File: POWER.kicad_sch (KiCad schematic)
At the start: 29 parts, among them J3 BAT_SOCKET, U4 BQ25185, U5 TPS62746, U8 TPS7A0533PDBV

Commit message: Adding outputs, updated some component values.
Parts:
- C11: value C -> 4.7UF
- D3: value D -> BAT54LP
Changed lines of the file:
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@@
 			)
 		)
-		(property "Value" "D"
+		(property "Value" "BAT54LP"
 			(at 181.61 138.43 0)
 			(effects
@@
 			)
 		)
-		(property "Value" "C"
+		(property "Value" "4.7UF"
 			(at 267.97 228.6062 0)
 			(effects

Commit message: removed backup zips. adding updated output files
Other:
- title: nRF Battery Dev Kit -> stm32_bluet_pill
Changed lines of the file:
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@@
 	(paper "A3")
 	(title_block
-		(title "nRF Battery Dev Kit")
-		(date "2024-02-26")
+		(title "stm32_bluet_pill")
+		(date "2024-04-03")
 		(rev "Proto")
 		(company "Clover Designs")

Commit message: updating design files
updating schematics, gerbers, design files, etc.
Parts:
- R16: value 1K -> 2.2K; Tol (none) -> 1%
- R17: Tol (none) -> 1%
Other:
- moved on the sheet: C25, L4, R17, R19

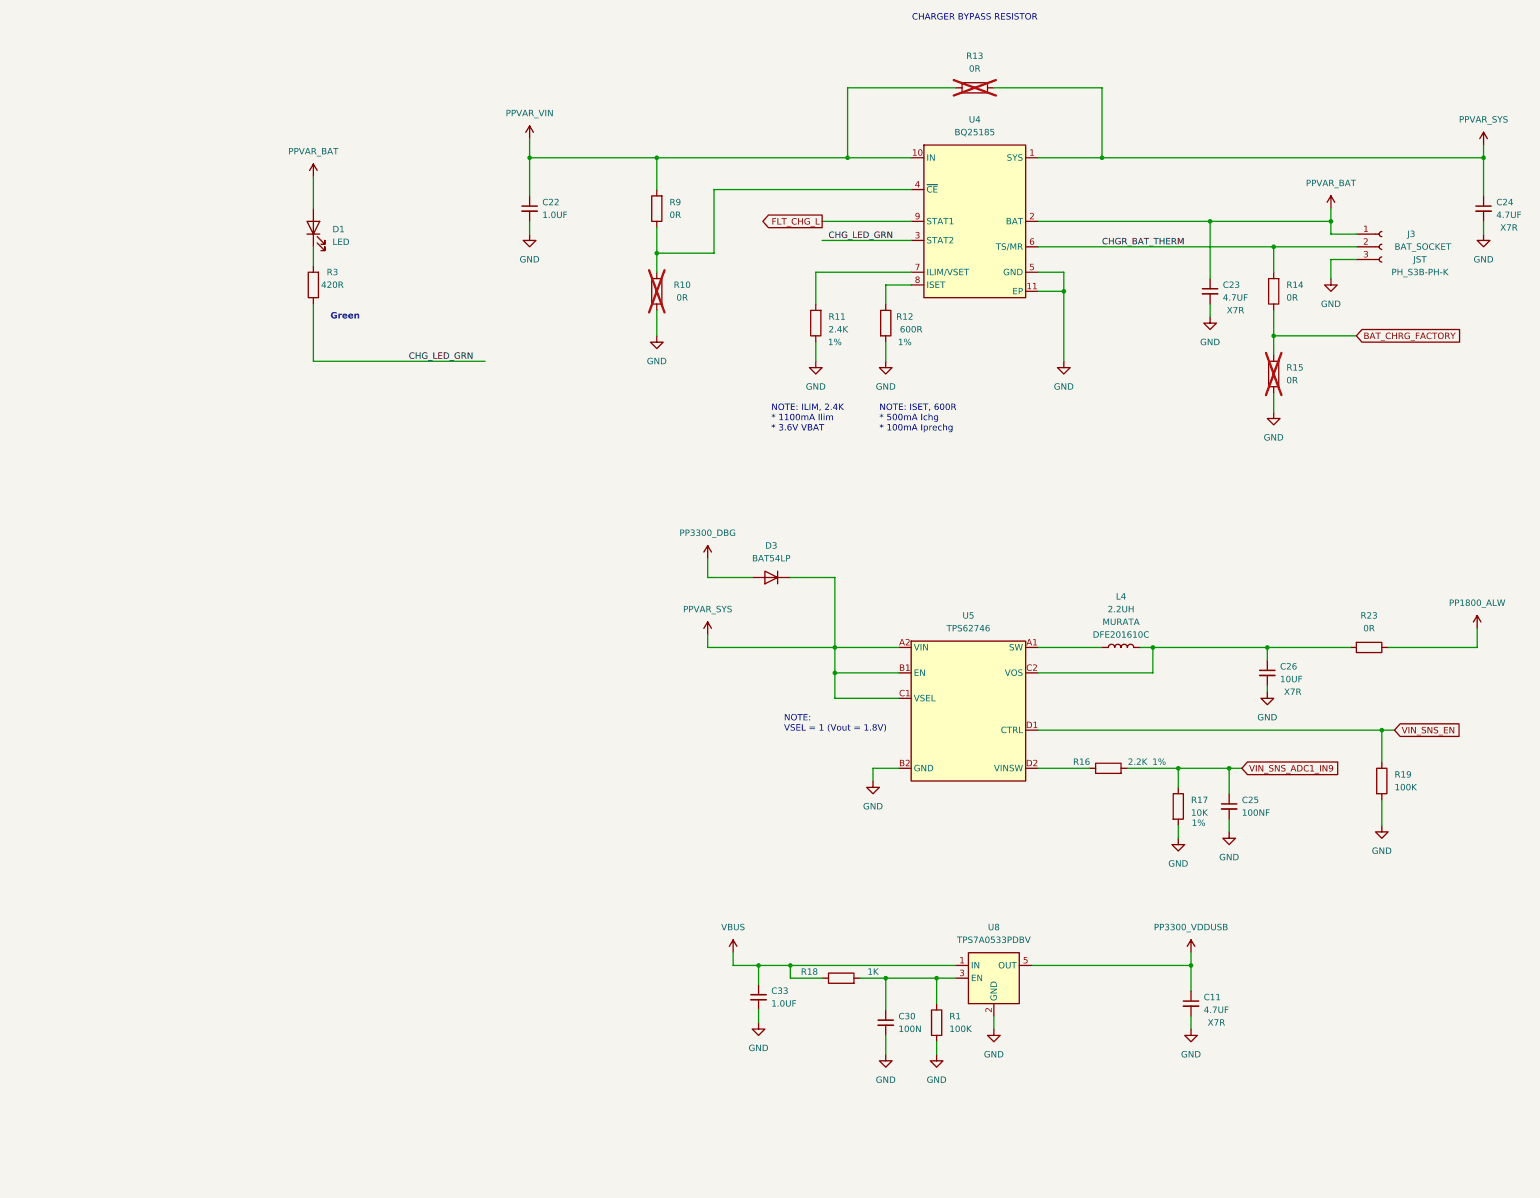
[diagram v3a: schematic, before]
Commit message: Updated project
- Changed board stackup, trace-widths
- Changed VIA size
- Fixed fab drawings
- added CHG FLT LED
- Removed unnecessary files
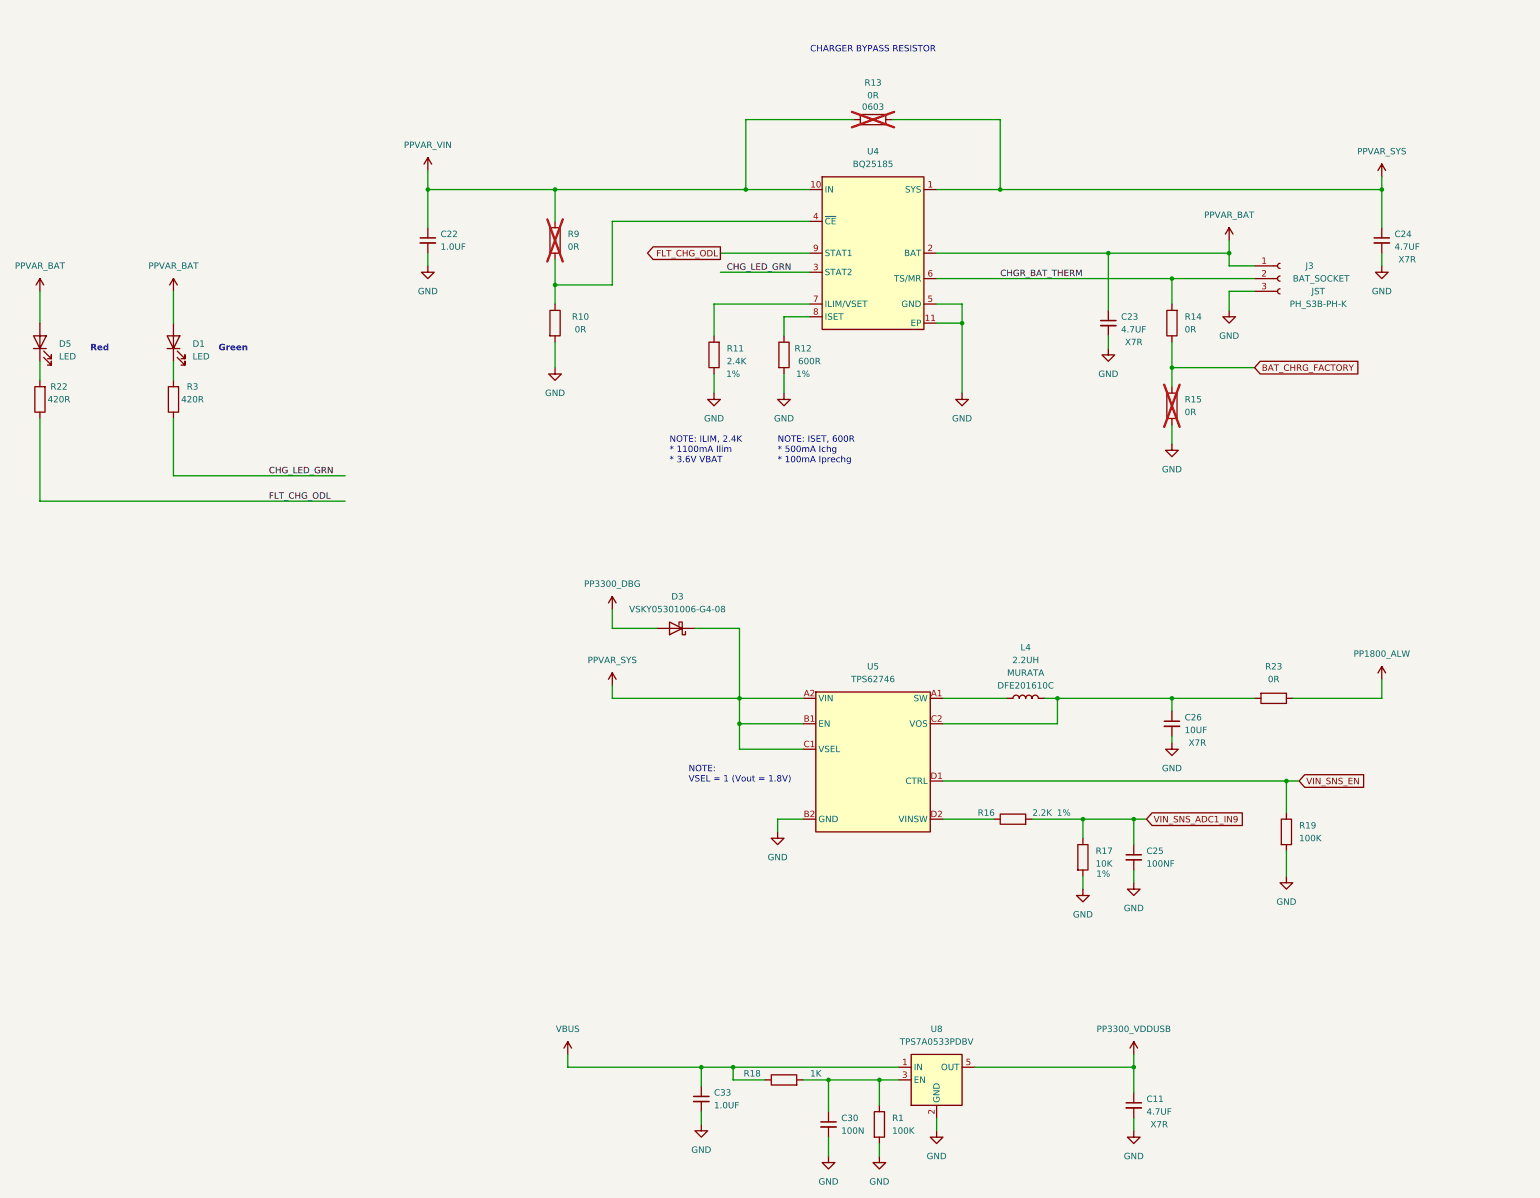
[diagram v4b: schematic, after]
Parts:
- added D5: LED, Diode_SMD:D_0402_1005Metric, symbol Device:LED
- added R22: 420R, Resistor_SMD:R_0201_0603Metric, symbol Device:R
- D3: value BAT54LP -> VSKY05301006-G4-08; symbol Device:D -> Device:D_Schottky
- R10: now fitted
- R13: footprint Resistor_SMD:R_0201_0603Metric -> Resistor_SMD:R_0603_1608Metric; PackType (none) -> 0603
- R9: now not fitted
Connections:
- net PPVAR_BAT: now also D5.2 (A)
- net FLT_CHG_L renamed FLT_CHG_ODL
- net FLT_CHG_ODL: now also R22.1
- new net: D5.1 (K), R22.2
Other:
- note added: "Red"
- company: Clover Designs -> Brendan Bleker
- moved on the sheet: C11, C22, C23, C24, C25, C26, C30, C33, D1, D3, J3, L4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

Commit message: Various BOM and Bug Fixes * Changed Stackup to common JLCPCB stackup * Modified trace widths as per new stackup * Reduced drill hole size * Rotated uFL connector as per datasheet pinout * Added pop options for ADC voltage * removed some GPIO and added GND to headers * BOM changes for battery charger, USB connector etc. to support component specifications and USB standards. * Improved MCU bypass and power delivery routing * Various other small bug fixes
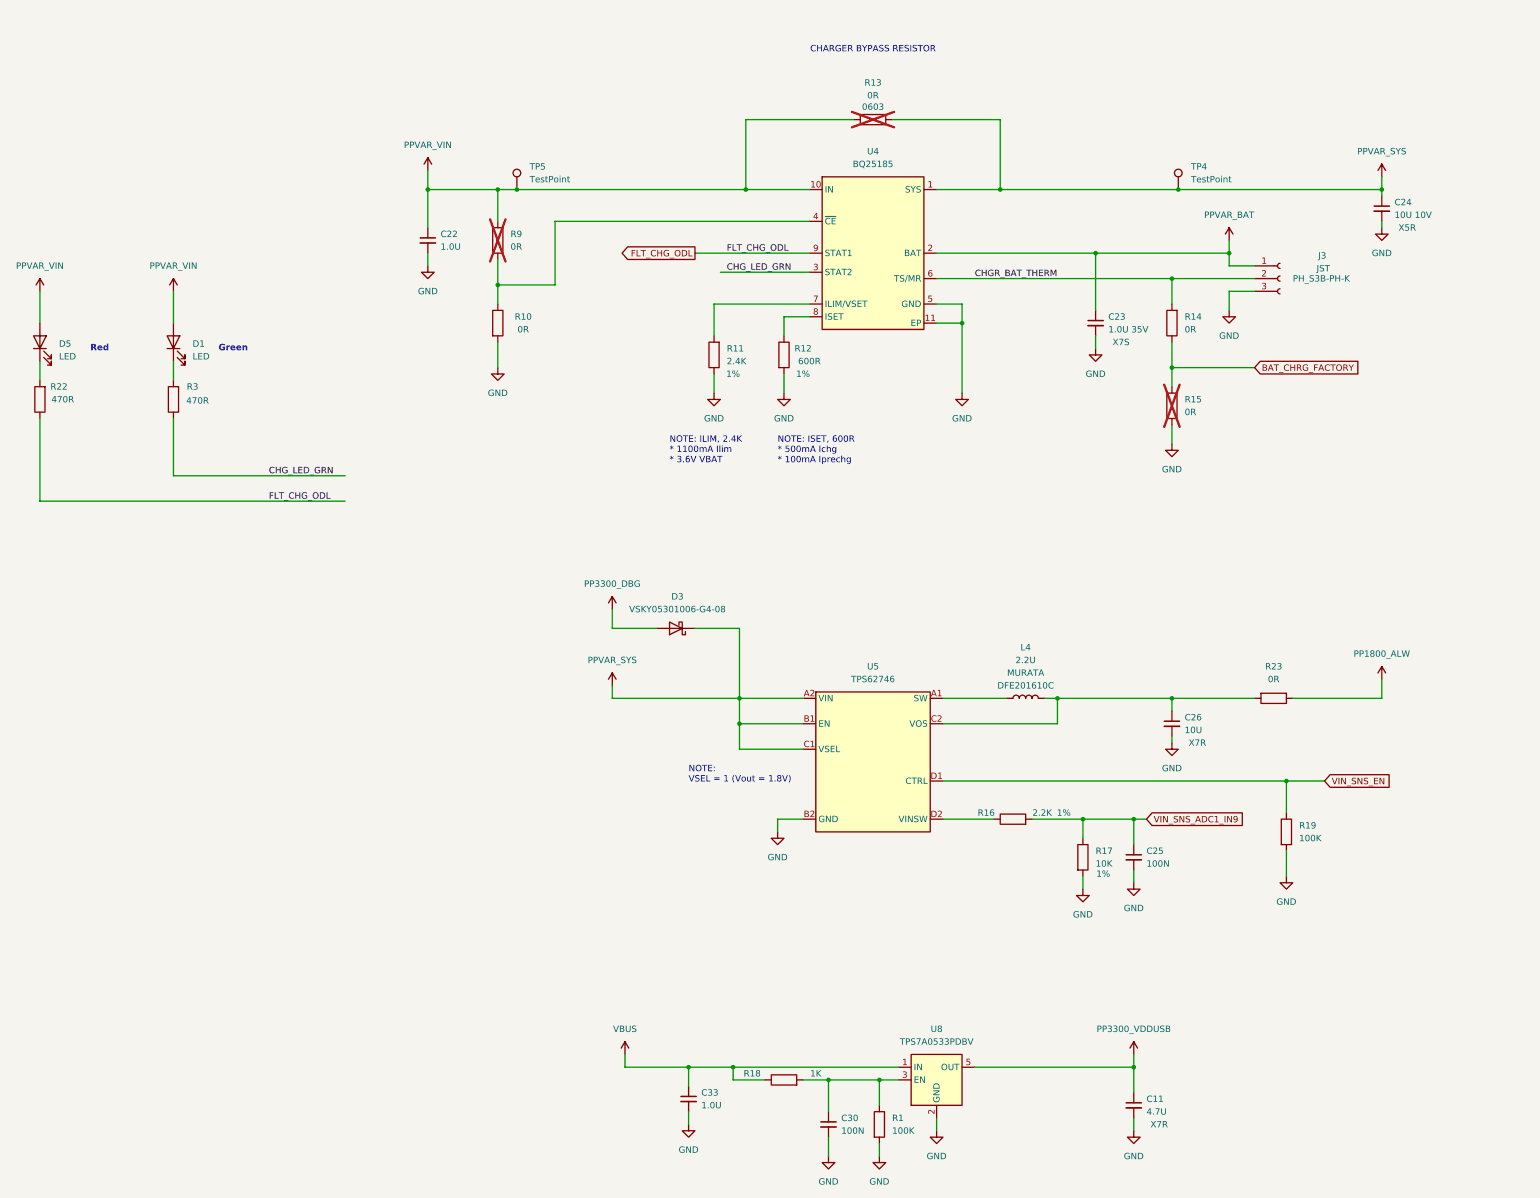
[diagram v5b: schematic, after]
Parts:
- added TP4, TP5: TestPoint, TestPoint:TestPoint_Pad_D1.0mm, symbol Connector:TestPoint
- C11: value 4.7UF -> 4.7U
- C22, C33: value 1.0UF -> 1.0U
- C23: value 4.7UF -> 1.0U 35V; DIELECTRIC X7R -> (none); MFR MURATA -> TDK; MFR_PN GRM155R61C475ME15 -> C1005JB1V105K050BC; TEMPCO (none) -> X7S
- C24: value 4.7UF -> 10U 10V; DIELECTRIC X7R -> (none); MFR MURATA -> Samsung; MFR_PN GRM155R61C475ME15 -> CL05A106MP8NUB8; TEMPCO (none) -> X5R
- C25: value 100NF -> 100N
- C26: value 10UF -> 10U
- C30: footprint Capacitor_SMD:C_0402_1005Metric -> Capacitor_SMD:C_0201_0603Metric
- J3: value BAT_SOCKET -> PH_S3B-PH-K
- L4: value 2.2UH -> 2.2U
- R22, R3: value 420R -> 470R
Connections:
- net PPVAR_BAT: no longer D1.2 (A), D5.2 (A)
- net PPVAR_SYS: now also TP4.1
- net PPVAR_VIN: now also D1.2 (A), D5.2 (A), TP5.1
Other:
- moved on the sheet: C23, C24, C33, R10, R9
